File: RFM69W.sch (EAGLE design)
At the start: 18 parts, among them U1 RFM69W, U2 MCP1701

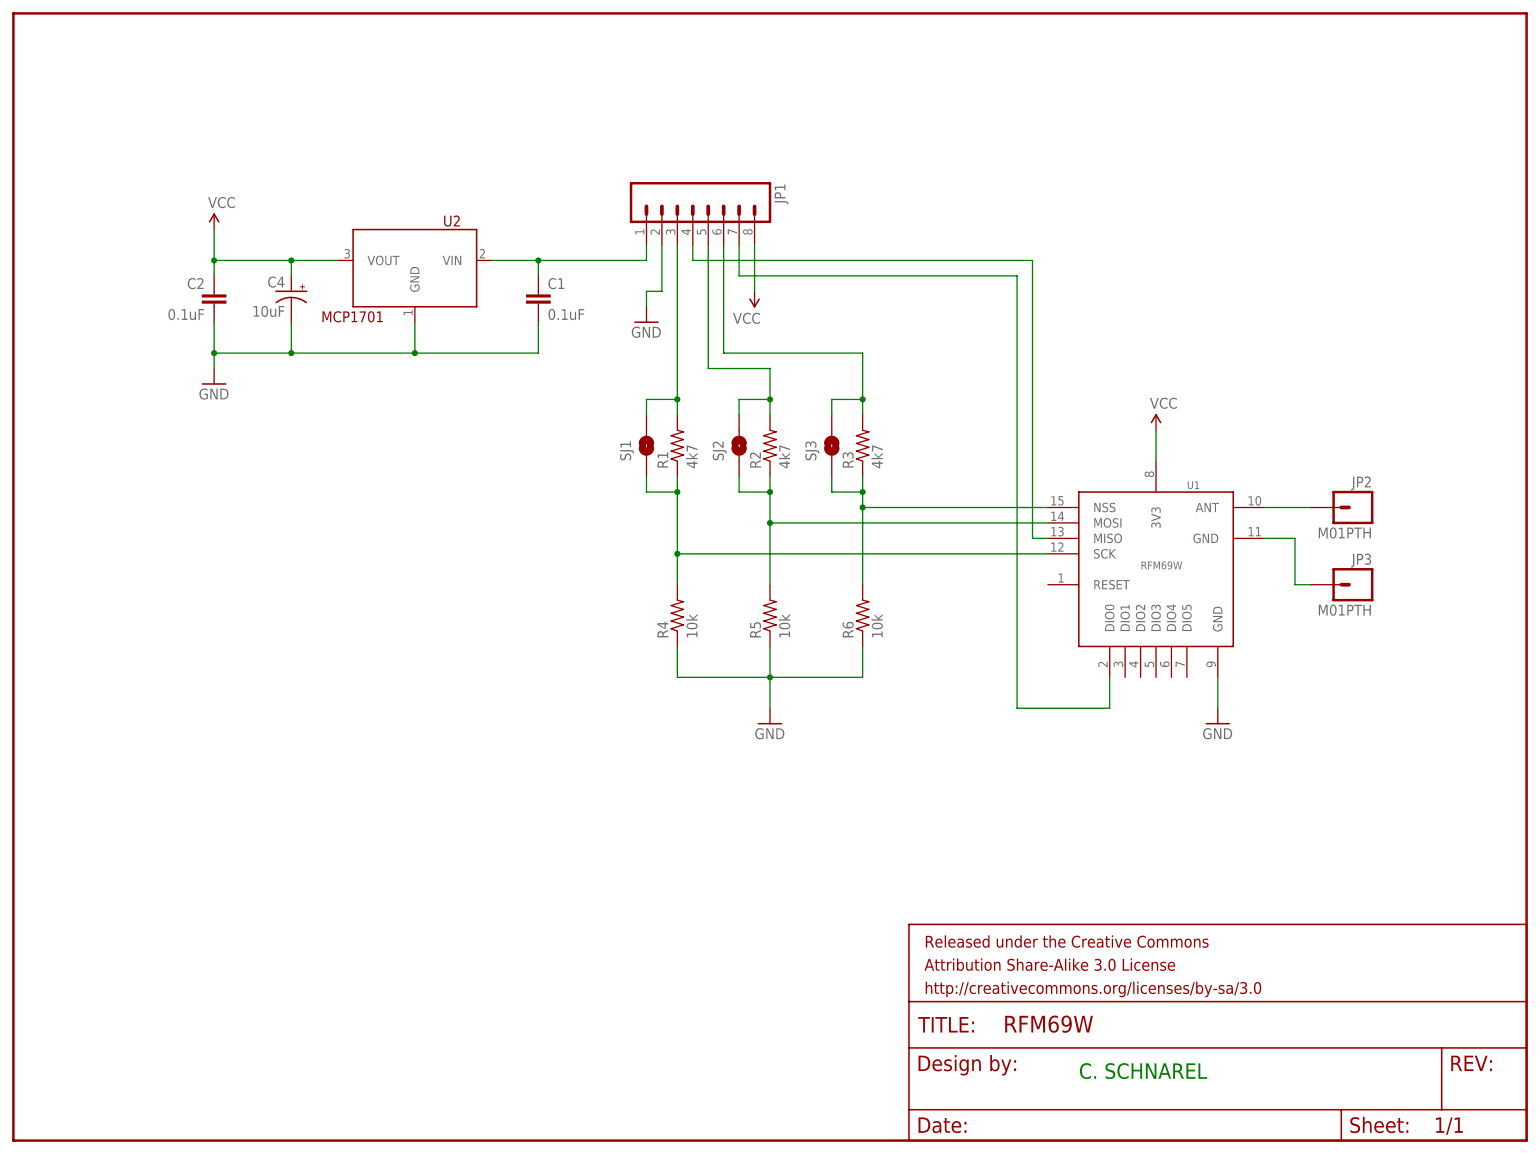
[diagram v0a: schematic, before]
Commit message: Combo Arduino Pro Mini and RFM69W
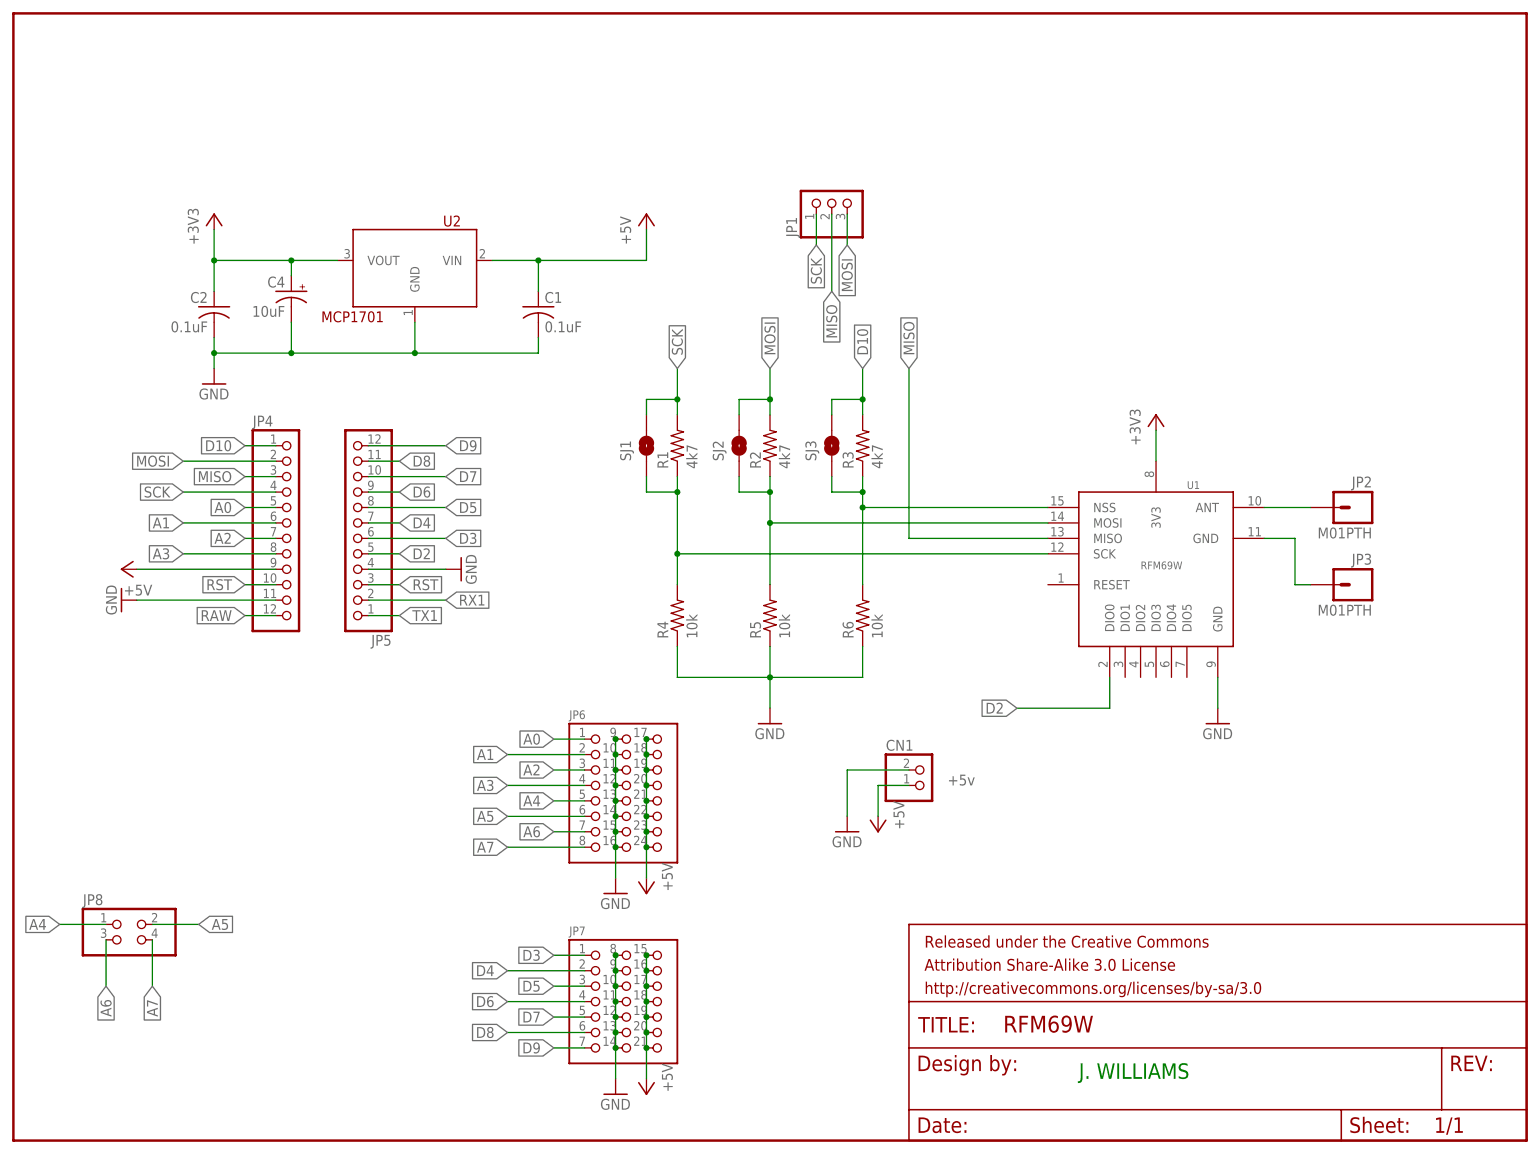
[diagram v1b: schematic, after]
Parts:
- added CN1: +5v, adafruit:JST_2PIN-THM-RA
- added JP4, JP5: (no value), pinhead:PINHD-1X12
- added JP6: PIN_3X8, pinhead_3row:PIN_3X8
- added JP7: PIN_3X7, pinhead_3row:PIN_3X7
- added JP8: (no value), pinhead:PINHD-2X2
- C1, C2: device SparkFun-Capacitors:CAP0805 -> rcl:C-USC1206
- C4: device ChipsParts:CAP_POL0805 -> resistor:CPOL-USA/3216-18R
- JP1: device SparkFun-Connectors:M08LONGPADS -> pinhead:PINHD-1X3
- R1, R2, R3, R4, R5, R6: device SparkFun-Resistors:RESISTOR0805-RES -> resistor:R-US_R1206
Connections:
- removed net N$2: C1.1, JP1.1, U2.VIN
- removed net N$3: JP1.4, U1.MISO
- removed net N$4: JP1.7, U1.DIO0
- removed net N$6: JP1.3, R1.2, SJ1.2
- removed net N$7: JP1.5, R2.2, SJ2.2
- removed net N$9: JP1.6, R3.2, SJ3.2
- removed net VCC: C2.1, C4.+, JP1.8, U1.3V3, U2.VOUT
- new net +3V3: C2.1, C4.+, U1.3V3, U2.VOUT
- new net +5V: C1.1, CN1.2, JP4.9, JP6.17, JP6.18, JP6.19, JP6.20, JP6.21, JP6.22, JP6.23, JP6.24, JP7.15, JP7.16, JP7.17, JP7.18, JP7.19, JP7.20, JP7.21, U2.VIN
- new net A0: JP4.5, JP6.1
- new net A1: JP4.6, JP6.2
- new net A2: JP4.7, JP6.3
- new net A3: JP4.8, JP6.4
- new net A4: JP6.5, JP8.1
- new net A5: JP6.6, JP8.2
- new net A6: JP6.7, JP8.3
- new net A7: JP6.8, JP8.4
- new net D10: JP4.1, R3.2, SJ3.2
- new net D2: JP5.5, U1.DIO0
- new net D3: JP5.6, JP7.1
- new net D4: JP5.7, JP7.2
- new net D5: JP5.8, JP7.3
- new net D6: JP5.9, JP7.4
- new net D7: JP5.10, JP7.5
- new net D8: JP5.11, JP7.6
- new net D9: JP5.12, JP7.7
- new net MISO: JP1.2, JP4.3, U1.MISO
- new net MOSI: JP1.3, JP4.2, R2.2, SJ2.2
- new net RAW: JP4.12
- new net RST: JP4.10, JP5.3
- new net RX1: JP5.2
- new net SCK: JP1.1, JP4.4, R1.2, SJ1.2
- new net TX1: JP5.1
- net GND: now also CN1.1, JP4.11, JP5.4, JP6.10, JP6.11, JP6.12, JP6.13, JP6.14, JP6.15, JP6.16, JP6.9, JP7.10, JP7.11, JP7.12, JP7.13, JP7.14, JP7.8, JP7.9; no longer JP1.2
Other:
- note added: "J. WILLIAMS"
- note removed: "C. SCHNAREL"
- moved on the sheet: C1, C2
